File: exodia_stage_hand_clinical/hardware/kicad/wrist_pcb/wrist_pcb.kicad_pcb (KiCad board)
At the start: 2 copper layers, 40 x 30 mm, 11 parts, among them J1 USBC_CONN, J2 ZIF_5PIN, Q1 IRLZ44N, Q2 2N7002, Q3 2N7002, Q4 2N7002, Q5 2N7002, U1 ESP32S3_MODULE, U2 TP4056_IC

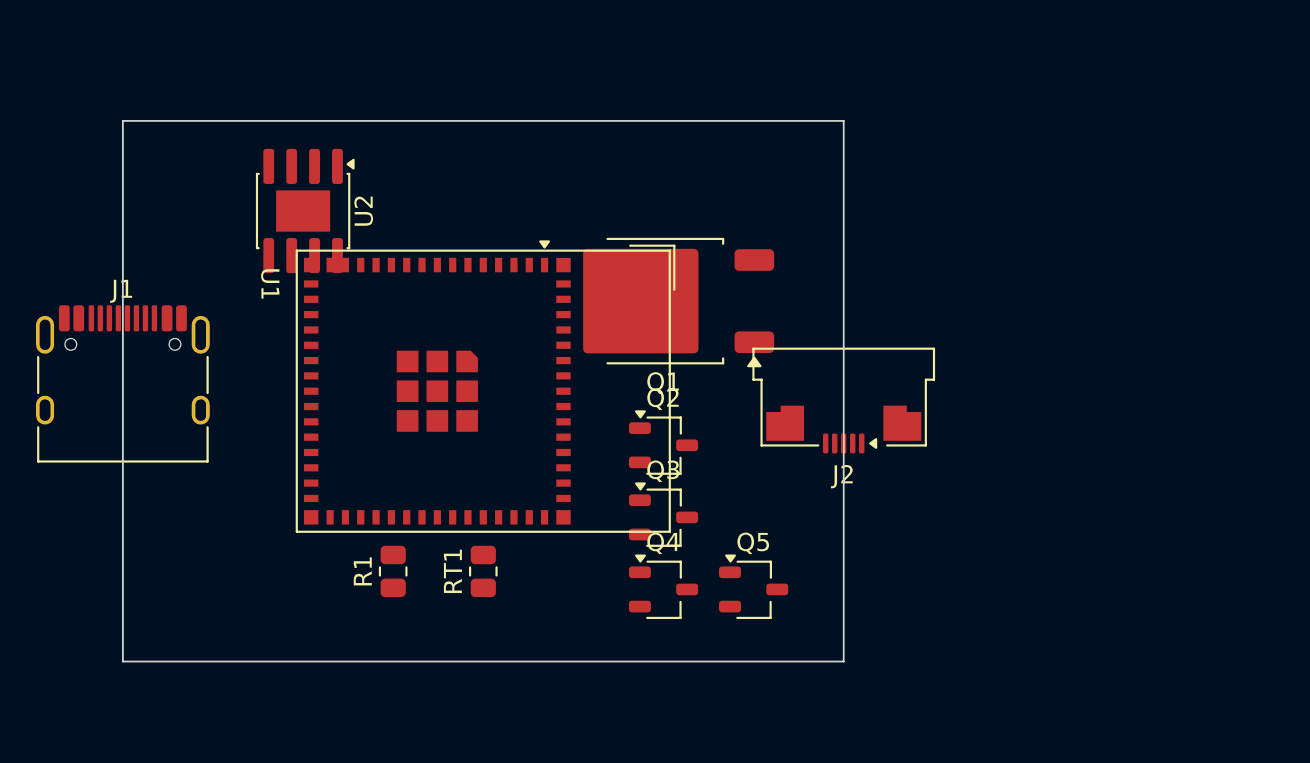
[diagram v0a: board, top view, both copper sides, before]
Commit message: Update physical ESP32 pin mappings (28/29/30/64/45) and exact USB pad mapping
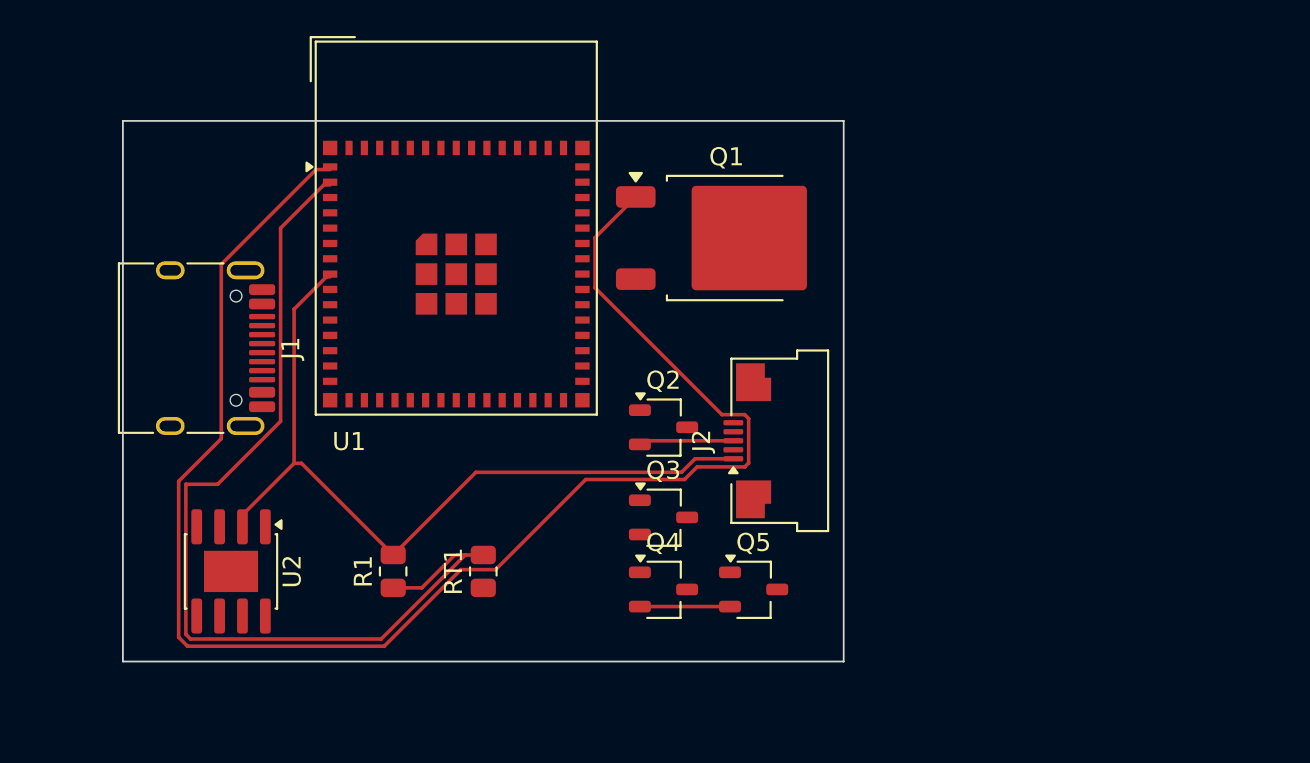
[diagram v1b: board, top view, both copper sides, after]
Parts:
- moved U2 20.4 mm to (106.0, 125.0)
- moved U1 9.17 mm to (118.5, 106.0), turned to 0 degrees
- moved Q1 4.95 mm to (133.5, 106.5), turned to 0 degrees
- moved J1 4.39 mm to (103.7, 112.6), turned to -90 degrees
- moved J2 4.24 mm to (136.8, 117.8), turned to 90 degrees
- moved Q2 1.00 mm to (130.0, 117.0)
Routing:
- net /PWM_HEATER: track 0.00 -> 85.9 mm
- net /ADC_NTC: track 0.00 -> 52.8 mm
- net /VCC: track 0.00 -> 44.7 mm
- net /NET_M_IDX: track 0.00 -> 5.27 mm
- net /NET_M_RNG_PNK: track 0.00 -> 5.00 mm

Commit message: Schematic v1.7: AO3400A Heater MOSFET, Netclasses (power_high, signal_data)
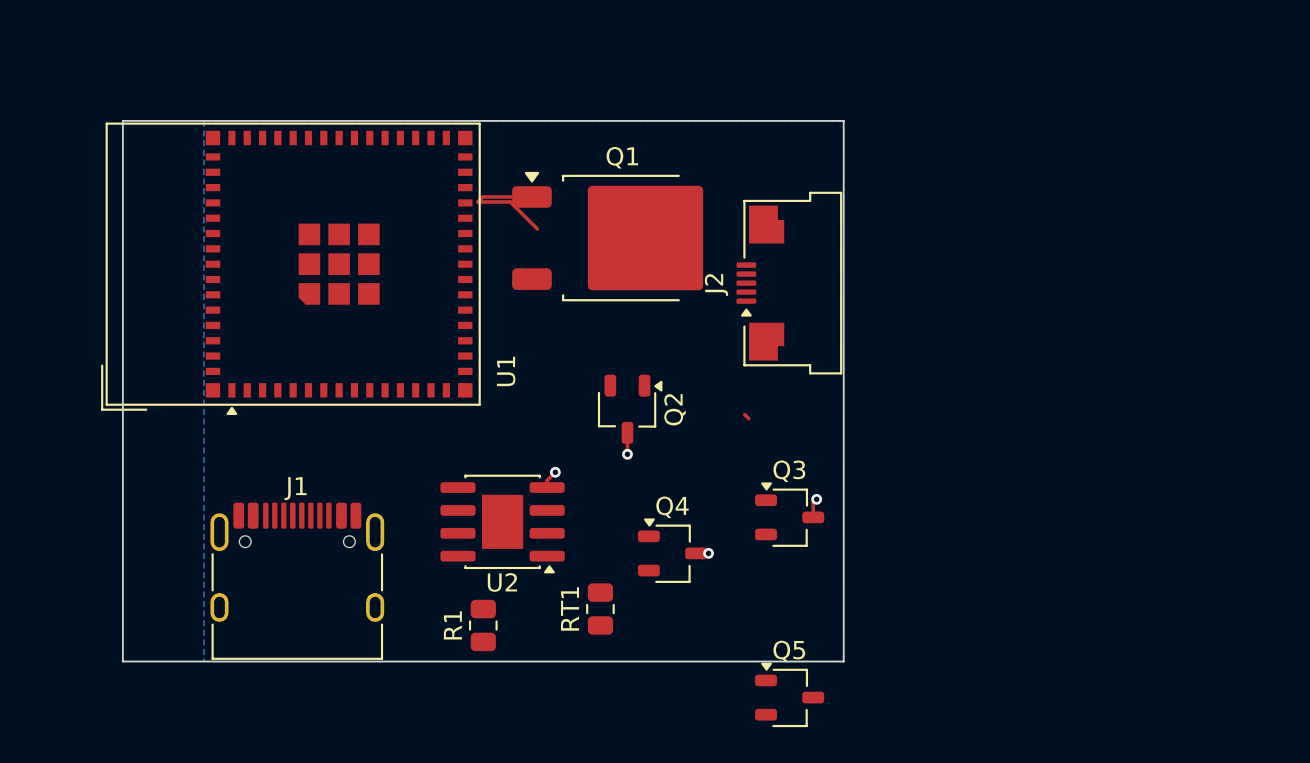
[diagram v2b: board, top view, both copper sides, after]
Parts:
- moved U2 15.3 mm to (121.1, 122.2), turned to 180 degrees
- moved J1 14.6 mm to (109.7, 126.0), turned to 0 degrees
- moved U1 9.27 mm to (109.5, 108.0), turned to 90 degrees
- moved J2 8.78 mm to (137.5, 109.0)
- moved Q3 7.00 mm to (137.0, 122.0)
- moved RT1 6.83 mm to (126.5, 127.1)
- moved Q5 6.32 mm to (137.0, 132.0)
- moved R1 5.83 mm to (120.0, 128.0)
- moved Q1 5.76 mm to (127.7, 106.5)
- moved Q2 2.24 mm to (128.0, 116.0), turned to -90 degrees
- moved Q4 2.06 mm to (130.5, 124.0)
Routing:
- net /PWM_HEATER: track 85.9 -> 8.35 mm
- net /ADC_NTC: track 52.8 -> 0.00 mm
- net /VCC: track 44.7 -> 0.00 mm
- net /NET_M_IDX: track 5.27 -> 0.00 mm
- net /NET_M_RNG_PNK: track 5.00 -> 0.00 mm
- net /GND: track 0.00 -> 3.99 mm, vias 0 -> 4
- added copper zone on B.Cu, net /GND

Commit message: Schematic v1.9: Re-mapped motor and heater gates to right-facing GPIOs (21-25) for optimized PCB routing
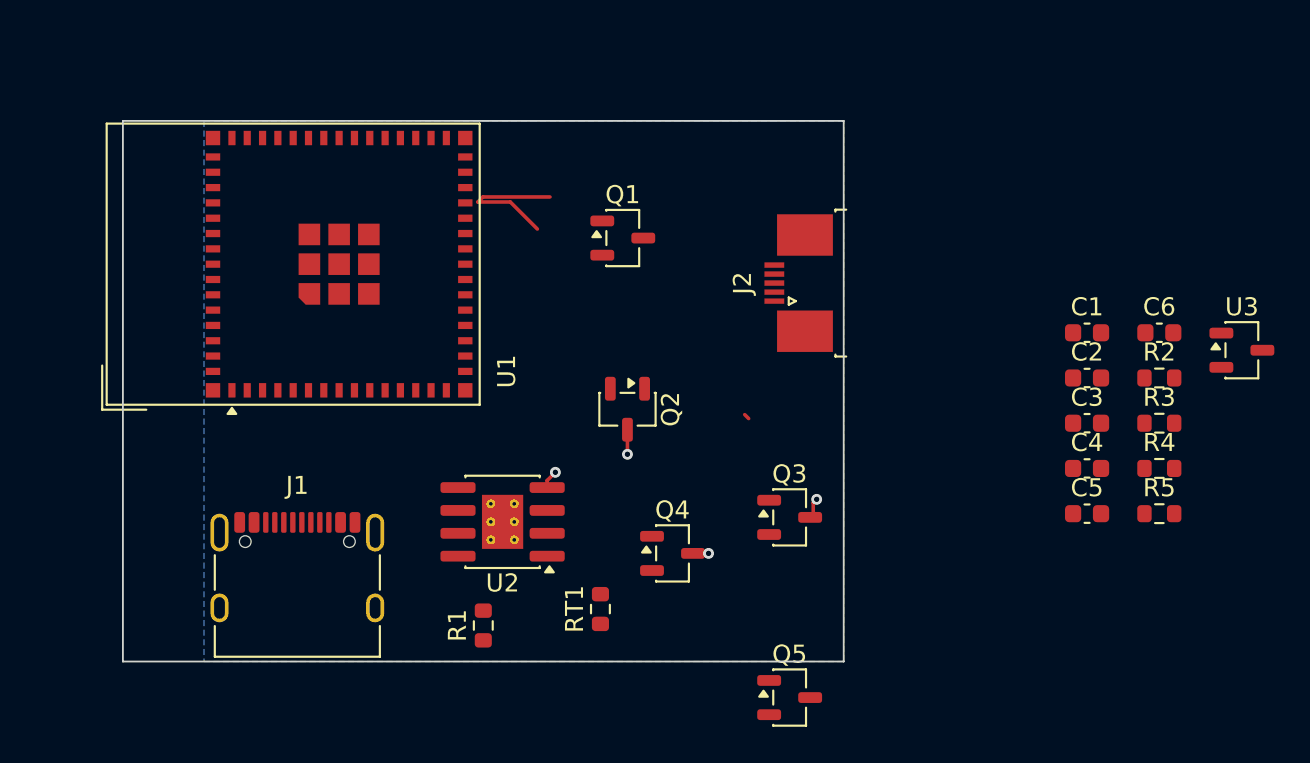
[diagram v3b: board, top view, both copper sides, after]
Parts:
- added C1: 10uF, Capacitor_SMD:C_0603_1608Metric, F.Cu at (153.5, 111.8)
- added C2: 10uF, Capacitor_SMD:C_0603_1608Metric, F.Cu at (153.5, 114.3)
- added C3: 1uF, Capacitor_SMD:C_0603_1608Metric, F.Cu at (153.5, 116.8)
- added C4: 1uF, Capacitor_SMD:C_0603_1608Metric, F.Cu at (153.5, 119.3)
- added C5: 10uF, Capacitor_SMD:C_0603_1608Metric, F.Cu at (153.5, 121.8)
- added C6: 0.1uF, Capacitor_SMD:C_0603_1608Metric, F.Cu at (157.5, 111.8)
- added R2: 100, Resistor_SMD:R_0603_1608Metric, F.Cu at (157.5, 114.3)
- added R3: 100K, Resistor_SMD:R_0603_1608Metric, F.Cu at (157.5, 116.8)
- added R4: 5.1K, Resistor_SMD:R_0603_1608Metric, F.Cu at (157.5, 119.3)
- added R5: 5.1K, Resistor_SMD:R_0603_1608Metric, F.Cu at (157.5, 121.8)
- added U3: AP2112K, Package_TO_SOT_SMD:SOT-23-3, F.Cu at (162.1, 112.7)
- J1: value USBC_CONN -> USBC_16PIN; footprint Connector_USB:USB_C_Receptacle_HRO_TYPE-C-31-M-12 -> Connector_USB:USB_C_Receptacle_XKB_U262-16XN-4BVC11
- J2: footprint Connector_FFC-FPC:Amphenol_F32Q-1A7x1-11005_1x05-1MP_P0.5mm_Horizontal -> Connector_FFC-FPC:TE_0-1734839-5_1x05-1MP_P0.5mm_Horizontal
- Q1: value IRLZ44N -> AO3400A; footprint Package_TO_SOT_SMD:TO-252-2 -> Package_TO_SOT_SMD:SOT-23-3
- Q2, Q3, Q4, Q5: footprint Package_TO_SOT_SMD:TSOT-23 -> Package_TO_SOT_SMD:SOT-23-3
- R1: value R_10K -> 10K; footprint Resistor_SMD:R_0805_2012Metric -> Resistor_SMD:R_0603_1608Metric
- RT1: footprint Resistor_SMD:R_0805_2012Metric -> Resistor_SMD:R_0603_1608Metric
- U2: footprint Package_SO:SOIC-8-1EP_3.9x4.9mm_P1.27mm_EP2.29x3mm -> Package_SO:SOIC-8-1EP_3.9x4.9mm_P1.27mm_EP2.29x3mm_ThermalVias
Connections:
- J1 pad A1: (no net) -> /GND
- J1 pad A12: (no net) -> /GND
- J1 pad A4: (no net) -> /VBUS
- J1 pad A5: (no net) -> /NET_CC1
- J1 pad A6: (no net) -> /USB_D+
- J1 pad A7: (no net) -> /USB_D-
- J1 pad A9: (no net) -> /VBUS
- J1 pad B1: (no net) -> /GND
- J1 pad B12: (no net) -> /GND
- J1 pad B4: (no net) -> /VBUS
- J1 pad B5: (no net) -> /NET_CC2
- J1 pad B9: (no net) -> /VBUS
- J1 pad SH: (no net) -> /GND
- J2 pad 1: /VCC -> /BAT+
- Q1 pad 1: /PWM_HEATER -> /GATE_HEAT
- Q1 pad 2: /NET_HEAT -> /GND
- Q1 pad 3: /GND -> /NET_HEAT
- Q2 pad 2: /NET_M_IDX -> /GND
- Q2 pad 3: /GND -> /NET_M_IDX
- Q3 pad 2: /NET_M_MID -> /GND
- Q3 pad 3: /GND -> /NET_M_MID
- Q4 pad 2: /NET_M_RNG_PNK -> /GND
- Q4 pad 3: /GND -> /NET_M_RNG_PNK
- Q5 pad 2: /NET_M_RNG_PNK -> /GND
- Q5 pad 3: /GND -> /NET_M_RNG_PNK
- R1 pad 2: /VCC -> /3V3
- U1 pad 1: /PWM_HEATER -> /GND
- U1 pad 2: /ADC_NTC -> /3V3
- U1 pad 20: (no net) -> /ADC_EMG
- U1 pad 26: (no net) -> /USB_D-
- U1 pad 27: (no net) -> /USB_D+
- U1 pad 3: /PWM_M_IDX -> (no net)
- U1 pad 38: (no net) -> /PWM_M_IDX
- U1 pad 39: (no net) -> /PWM_M_MID
- U1 pad 4: /PWM_M_MID -> (no net)
- U1 pad 40: (no net) -> /PWM_M_RNG
- U1 pad 41: (no net) -> /PWM_M_PNK
- U1 pad 42: (no net) -> /PWM_HEATER
- U1 pad 5: /PWM_M_RNG -> (no net)
- U1 pad 6: /PWM_M_PNK -> (no net)
- U1 pad 7: /ADC_EMG -> (no net)
- U1 pad 8: /VCC -> /ADC_NTC
- U1 pad 9: /GND -> (no net)
- U2 pad 1: /VBUS -> (no net)
- U2 pad 2: /VCC -> (no net)
- U2 pad 4: /GND -> /VBUS
- U2 pad 5: (no net) -> /BAT+
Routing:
- net /GND: track 3.99 -> 0.00 mm, vias 4 -> 0
- net /NET_M_IDX: track 0.00 -> 1.19 mm, vias 0 -> 1
- net /NET_M_MID: track 0.00 -> 1.08 mm, vias 0 -> 1
- net /VBUS: track 0.00 -> 1.03 mm, vias 0 -> 1
- net /NET_M_RNG_PNK: track 0.00 -> 0.69 mm, vias 0 -> 1

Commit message: Schematic v1.10: Reverted Q4 (PWM_M_RNG) back to Pin 40 to preserve active trace, other pins kept on safe 21-25
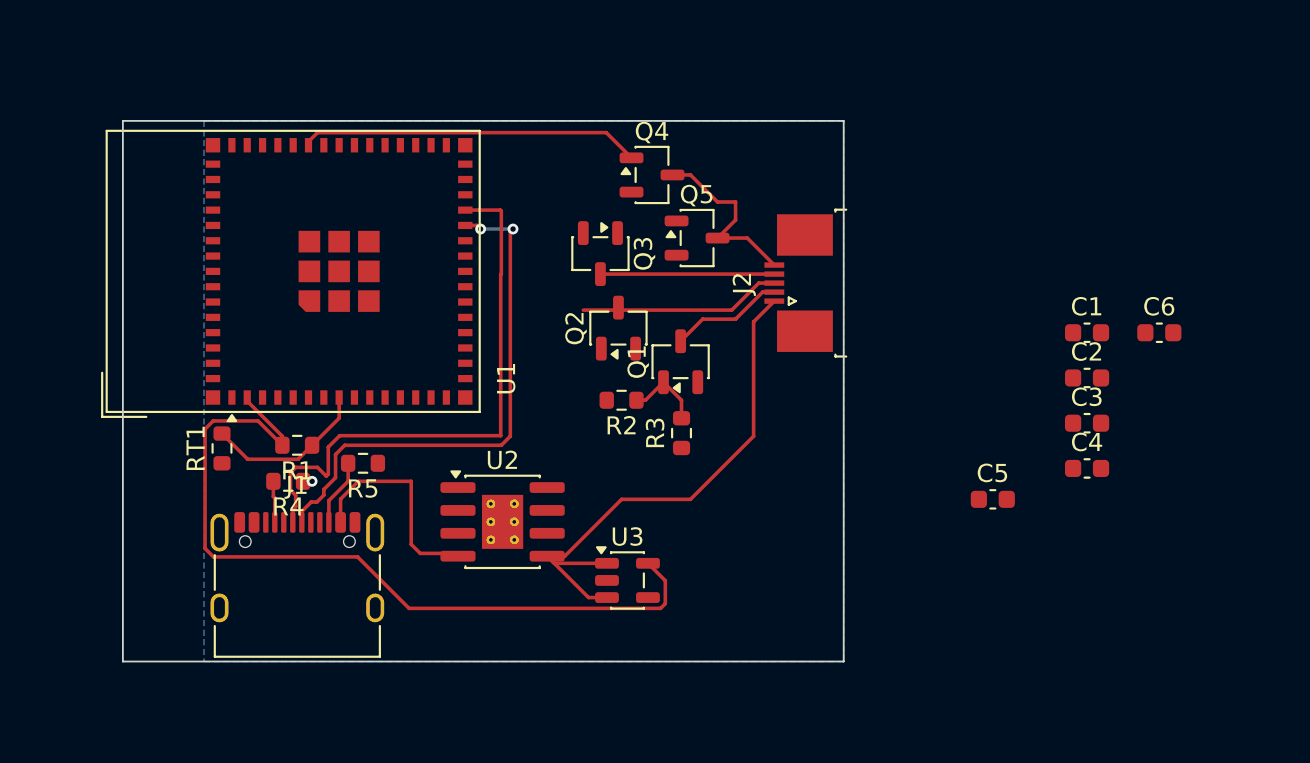
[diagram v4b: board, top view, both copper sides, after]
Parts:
- U3: footprint Package_TO_SOT_SMD:SOT-23-3 -> Package_TO_SOT_SMD:SOT-23-5
- moved R4 48.3 mm to (109.2, 120.0), turned to 180 degrees
- moved R5 44.3 mm to (113.3, 119.0), turned to 180 degrees
- moved U3 36.4 mm to (128.0, 125.5)
- moved R2 29.9 mm to (127.7, 115.5), turned to 180 degrees
- moved R3 26.5 mm to (131.0, 117.3), turned to 90 degrees
- moved Q5 26.0 mm to (131.9, 106.5)
- moved RT1 22.8 mm to (105.5, 118.2)
- moved Q4 21.0 mm to (129.4, 103.0)
- moved Q3 18.0 mm to (126.5, 107.4), turned to -90 degrees
- moved R1 14.4 mm to (109.7, 118.0), turned to 180 degrees
- moved Q1 7.58 mm to (130.9, 113.4), turned to 90 degrees
- moved C5 5.29 mm to (148.3, 121.0)
- moved Q2 4.53 mm to (127.5, 111.5), turned to 90 degrees
- moved U1 0.40 mm to (109.5, 108.3)
- turned U2 to 0 degrees
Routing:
- net /3V3: track 0.00 -> 44.8 mm
- net /USB_D+: track 0.00 -> 31.3 mm
- net /BAT+: track 0.00 -> 30.3 mm
- net /USB_D-: track 0.00 -> 29.1 mm, vias 0 -> 2
- net /PWM_M_RNG: track 0.00 -> 18.9 mm
- net /VBUS: track 1.03 -> 12.0 mm, vias 1 -> 0
- net /NET_M_IDX: track 1.19 -> 11.2 mm, vias 1 -> 0
- net /NET_M_RNG_PNK: track 0.69 -> 10.3 mm, vias 1 -> 0
- net /ADC_NTC: track 0.00 -> 9.18 mm
- net /NET_M_MID: track 1.08 -> 9.65 mm, vias 1 -> 0
- net /PWM_HEATER: track 8.35 -> 0.00 mm
- net /NET_HEAT: track 0.00 -> 6.33 mm
- net /GATE_HEAT: track 0.00 -> 4.33 mm
- net /NET_CC2: track 0.00 -> 3.72 mm
- net /NET_CC1: track 0.00 -> 2.31 mm
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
